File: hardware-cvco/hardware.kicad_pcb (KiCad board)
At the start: 4 copper layers, 99 x 75 mm, 159 parts, among them J1 SMA, J2 SMA, J3 SMA, J4 SMA, J5 SMA, J6 SMA, J7 SMA, J8 Pickit 2, J9 DC, Q1 AOD403, Q2 MBT2222, SW1 On/Off, U1 74LS07, U10 TPS61046, U11 BQ21040, U12 LM358, U13 LM317DCYR, U14 LM386, U2 NLB-310-T1, U3 NLB-310-T1, U4 NLB-310-T1, U5 NLB-310-T1, U6 PIC12F675-ISN, U7 NLB-310-T1, U8 NLB-310-T1, U9 NLB-310-T1, Y1 CVCO55CW-0100-0200, Y2 CVCO55CW-0200-0500, Y3 CV55CW500-1000, Y4 CVCO55CW-1000-2000, Y5 CV55BE1600-3200, Y6 CVCO55CC-3180-3710, Y7 CVCO55CW-3500-4500

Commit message: Replaced FA icons.
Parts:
- added G***: Thermometer, Icons:Thermometer, F.Cu at (97.3, 117.3)
- added G***: Switch, Icons:Switch, F.Cu at (83.8, 117.3)
- added G***: Lightbulb, Icons:Lightbulb, F.Cu at (110.6, 117.3)
- added G***: Lightbulb, Icons:Lightbulb, F.Cu at (103.7, 117.3)
- added G***: Lightning, Icons:Lightning, F.Cu at (68.0, 121.0)
- added G***: LOGO, Icons:Battery, F.Cu at (90.6, 117.5)
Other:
- board text added: "CHG"
- board text added: "PWR"

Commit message: Replaced LM358 with LM324.
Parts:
- removed G***: Thermometer, Icons:Thermometer
- removed G***: Switch, Icons:Switch
- removed G*** (x2): Lightbulb, Icons:Lightbulb
- removed G***: Lightning, Icons:Lightning
- removed G***: LOGO, Icons:Battery
- added R53: 2k, Resistor_SMD:R_0805_2012Metric_Pad1.15x1.40mm_HandSolder, B.Cu at (141.3, 115.0)
- added R54: 2k, Resistor_SMD:R_0805_2012Metric_Pad1.15x1.40mm_HandSolder, B.Cu at (141.3, 112.1)
- R17: value 100 -> 1k
- R33: value 15k -> 120
- R34: value 120 -> 680
- U12: value LM358 -> LM324; footprint Package_SO:SO-8_5.3x6.2mm_P1.27mm -> Package_SO:SOIC-14_3.9x8.7mm_P1.27mm
- moved U12 0.43 mm to (134.7, 111.3), turned to 0 degrees
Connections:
- R17 pad 1: Tuner -> Net-(R17-Pad1)
- R18 pad 1: Tuner -> Net-(R17-Pad1)
- U12 pad 4: P2_VSS -> P2_VDD
- U12 pad 8: P2_VDD -> Tuner

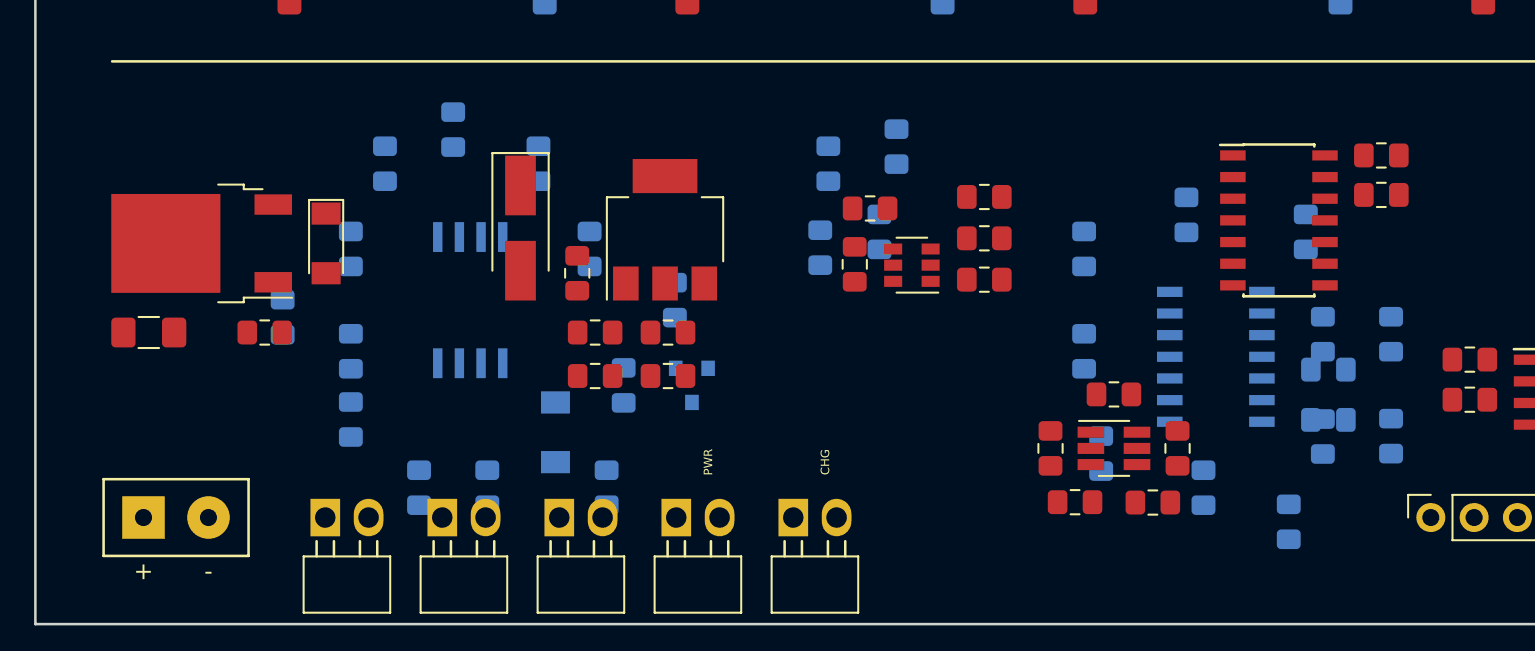
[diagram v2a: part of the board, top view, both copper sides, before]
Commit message: Non-RF section layout finished - CVCO.
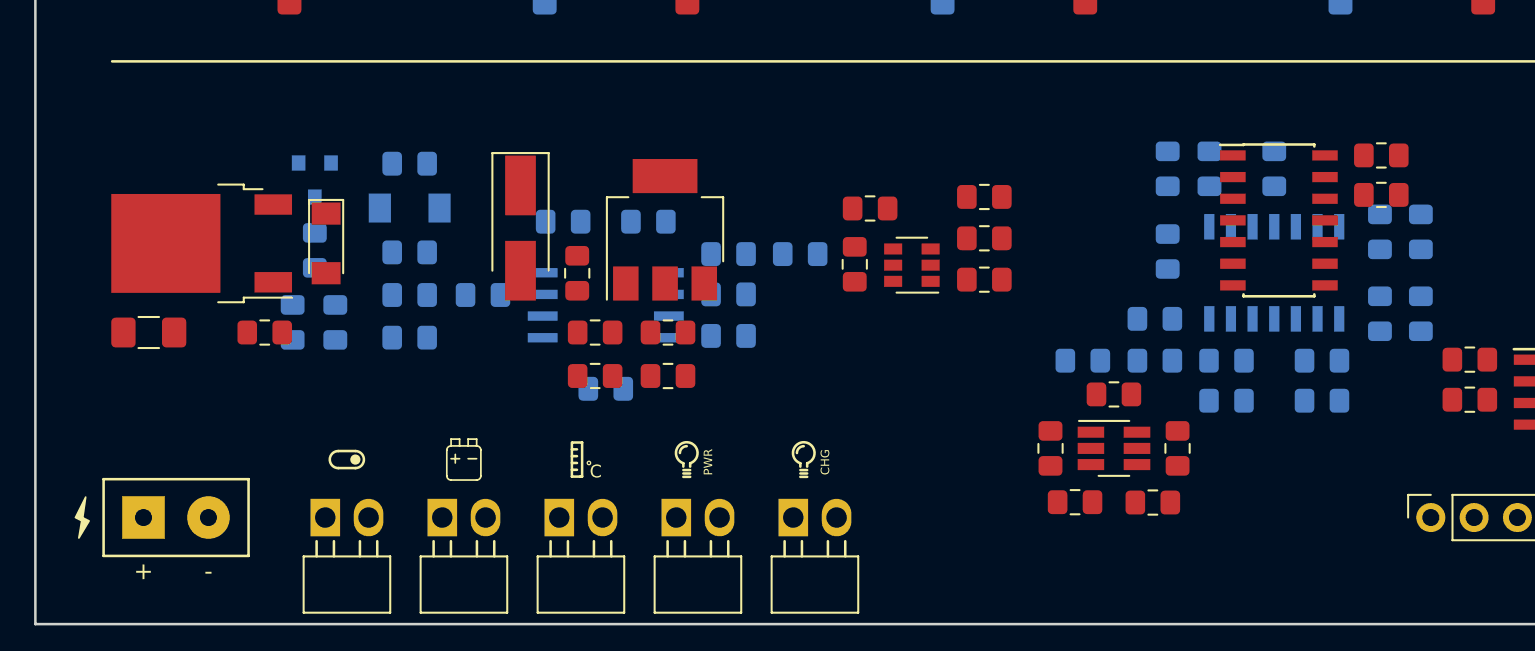
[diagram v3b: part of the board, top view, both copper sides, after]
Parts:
- added G***: Lightbulb, Icons:Lightbulb, F.Cu at (110.6, 117.4)
- added G***: Lightbulb, Icons:Lightbulb, F.Cu at (103.7, 117.4)
- added G***: Thermometer, Icons:Thermometer, F.Cu at (97.3, 117.3)
- added G***: Battery, Icons:Battery, F.Cu at (90.6, 117.5)
- added G***: Switch, Icons:Switch, F.Cu at (83.8, 117.3)
- added G***: Lightning, Icons:Lightning, F.Cu at (68.2, 121.0)
- moved Q2 25.2 mm to (81.9, 101.0)
- moved C47 22.3 mm to (106.2, 107.7), turned to 0 degrees
- moved C48 22.2 mm to (106.2, 110.1), turned to 0 degrees
- moved R17 18.9 mm to (126.9, 111.5), turned to 0 degrees
- moved R35 18.6 mm to (83.1, 109.3), turned to 90 degrees
- moved C54 18.2 mm to (101.5, 103.4), turned to 180 degrees
- moved R40 17.9 mm to (80.6, 109.3), turned to 90 degrees
- moved C13 17.8 mm to (131.2, 111.5), turned to 0 degrees
- moved R50 17.7 mm to (96.5, 103.4), turned to 180 degrees
- moved R52 17.1 mm to (131.9, 100.3)
- moved R37 16.5 mm to (140.9, 113.9), turned to 0 degrees
- moved R53 16.3 mm to (134.3, 100.3), turned to 90 degrees
- moved D12 15.7 mm to (87.5, 102.6), turned to 180 degrees
- moved R45 15.6 mm to (87.5, 107.7), turned to 180 degrees
- moved C58 15.1 mm to (99.0, 113.2), turned to 180 degrees
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
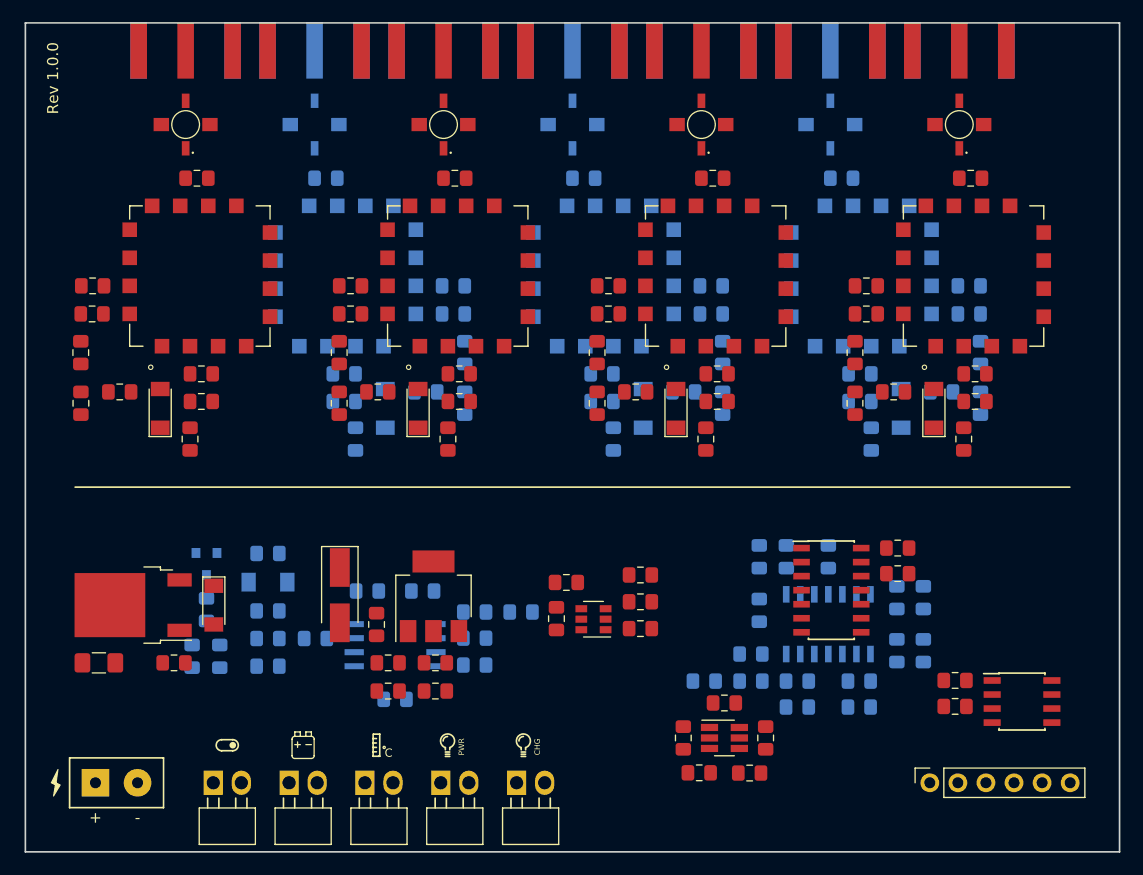
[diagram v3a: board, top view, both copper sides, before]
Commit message: RF section routing - CVCO.
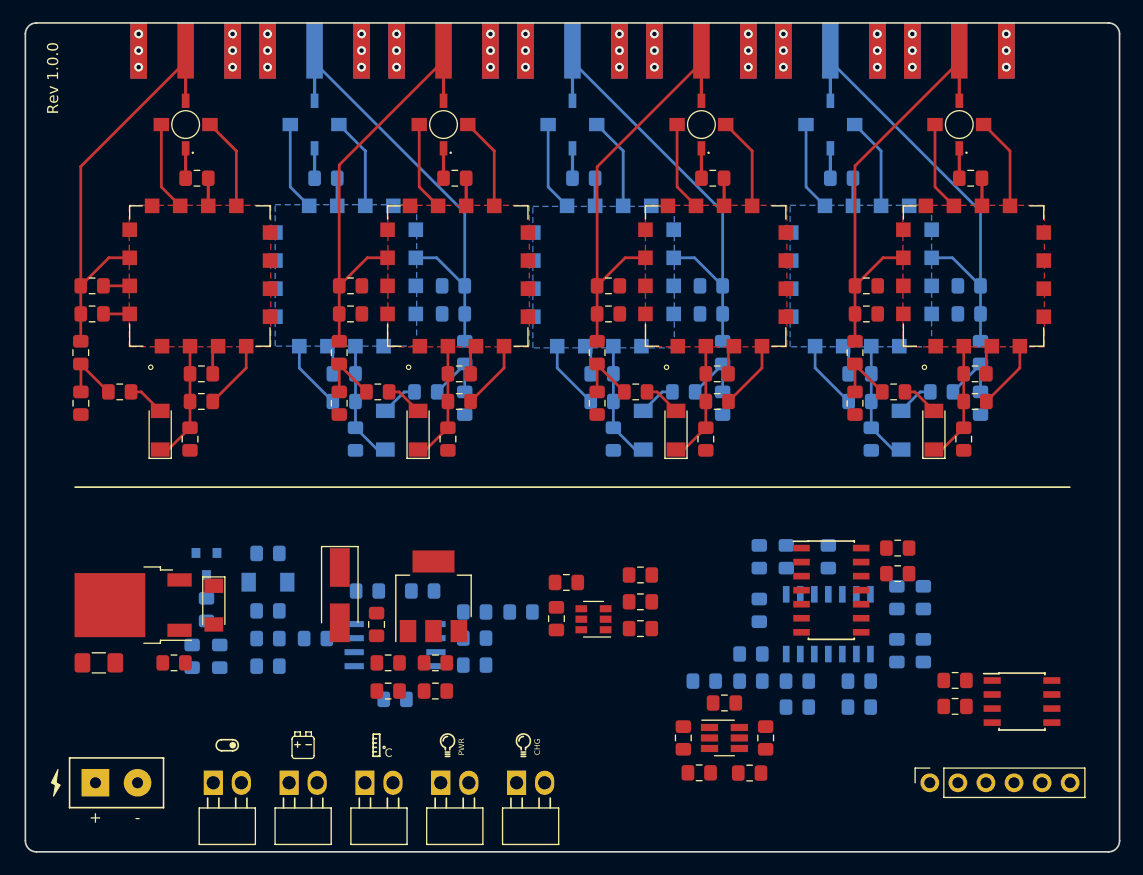
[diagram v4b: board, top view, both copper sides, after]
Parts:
- moved D1 1.97 mm to (77.7, 88.8)
- moved D2 1.97 mm to (101.0, 88.8)
- moved D3 1.97 mm to (124.4, 88.8)
- moved D4 1.97 mm to (147.7, 88.8)
- moved D5 1.97 mm to (98.1, 88.8)
- moved D6 1.97 mm to (121.4, 88.8)
- moved D7 1.97 mm to (144.7, 88.8)
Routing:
- net P2_VSS: track 0.00 -> 205.7 mm, vias 0 -> 42
- net Net-(C31-Pad1): track 0.00 -> 42.0 mm
- net Net-(C29-Pad1): track 0.00 -> 42.0 mm
- net Net-(C27-Pad1): track 0.00 -> 42.0 mm
- net Net-(C1-Pad1): track 0.00 -> 40.3 mm
- net Net-(C3-Pad1): track 0.00 -> 40.2 mm
- net Net-(C7-Pad1): track 0.00 -> 40.2 mm
- net Net-(C5-Pad1): track 0.00 -> 40.2 mm
- net VT_4: track 0.00 -> 10.9 mm
- net VT_5: track 0.00 -> 10.9 mm
- net VT_2: track 0.00 -> 10.9 mm
- net VT_1: track 0.00 -> 10.9 mm
- net VT_6: track 0.00 -> 10.9 mm
- net VT_7: track 0.00 -> 10.9 mm
- net VT_3: track 0.00 -> 10.9 mm
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- added copper zone on B.Cu, net P2_VSS
- added copper zone on F.Cu, net P2_VSS
- added copper zone on In1.Cu, net P2_VSS
- added copper zone on In2.Cu, net P2_VSS
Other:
- outline, holes or cut-outs redrawn

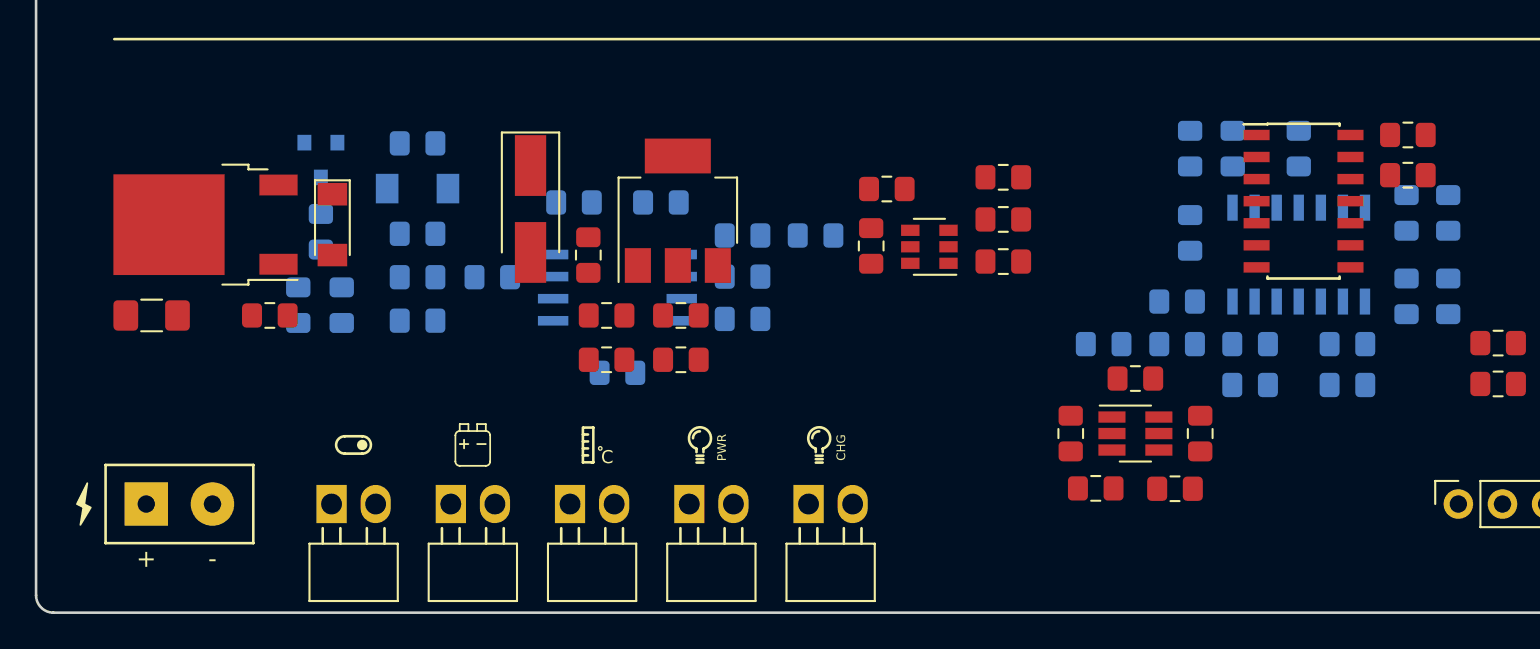
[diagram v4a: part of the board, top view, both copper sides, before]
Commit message: Power Supply & Battery Management routing - CVCO.
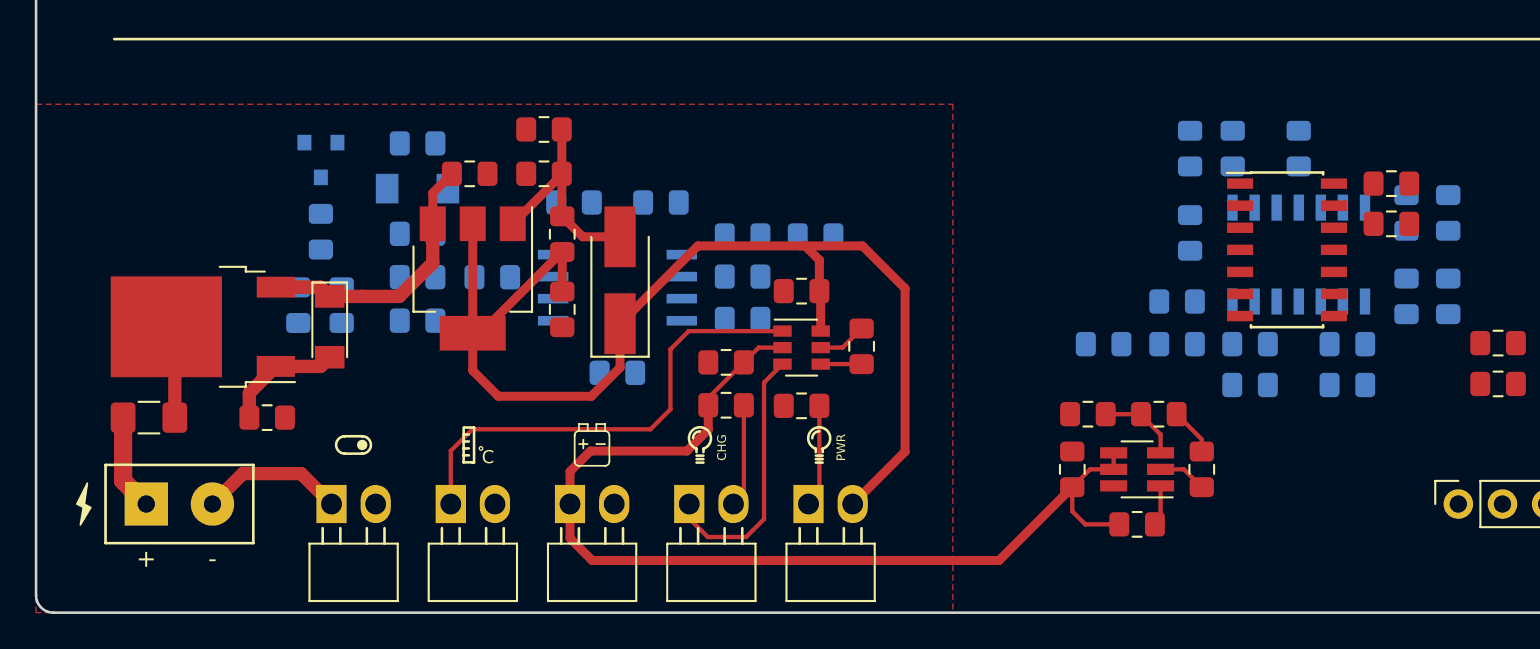
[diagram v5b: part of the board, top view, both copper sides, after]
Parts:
- F1: value 3A Fast -> 2.5A Fast
- moved R33 20.7 mm to (105.2, 115.1)
- moved C45 17.9 mm to (105.2, 112.6), turned to 180 degrees
- moved C51 14.6 mm to (90.5, 101.8), turned to 0 degrees
- moved R36 14.3 mm to (109.5, 115.1), turned to 180 degrees
- moved C57 13.7 mm to (94.7, 99.2), turned to 180 degrees
- moved U13 12.4 mm to (90.6, 107.8), turned to 270 degrees
- moved U11 9.37 mm to (109.5, 111.8), turned to 0 degrees
- moved R34 9.17 mm to (113.0, 111.7), turned to 90 degrees
- moved R49 8.91 mm to (94.7, 101.8), turned to 180 degrees
- moved L1 8.39 mm to (128.8, 121.9), turned to 180 degrees
- moved C36 7.82 mm to (132.6, 118.8), turned to 270 degrees
- moved C43 7.64 mm to (125.1, 118.8), turned to 90 degrees
- moved C52 7.42 mm to (95.8, 109.5), turned to 270 degrees
- moved D8 6.86 mm to (109.9, 120.8)
- moved D9 6.86 mm to (103.1, 120.8)
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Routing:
- net DC: track 0.00 -> 69.2 mm
- net BAT: track 0.00 -> 60.0 mm
- net Net-(TH1-Pad1): track 0.00 -> 27.0 mm
- net Net-(C51-Pad1): track 0.00 -> 15.6 mm
- net Net-(D9-Pad1): track 0.00 -> 15.4 mm
- net Net-(C57-Pad1): track 0.00 -> 12.9 mm
- net Net-(J9-Pad2): track 0.00 -> 8.30 mm
- net Net-(D10-Pad2): track 0.00 -> 6.90 mm
- net Net-(D9-Pad2): track 0.00 -> 5.93 mm
- net Net-(D8-Pad1): track 0.00 -> 5.91 mm
- net P2_VSS: track 205.7 -> 211.3 mm
- net Net-(F1-Pad1): track 0.00 -> 5.52 mm
- net Net-(F1-Pad2): track 0.00 -> 5.43 mm
- net Net-(R31-Pad2): track 0.00 -> 4.72 mm
- net P2_VDD: track 0.00 -> 2.75 mm
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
